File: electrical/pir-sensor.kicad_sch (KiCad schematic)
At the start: 6 parts, among them J6 0705430002

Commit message: Layout complete
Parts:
- J6: FT Rotation Offset (none) -> 90
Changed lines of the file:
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@@
 			)
 		)
-		(property "Datasheet" ""
+		(property "Datasheet" "https://www.molex.com/pdm_docs/sd/705430001_sd.pdf"
 			(at 100.33 78.74 0)
 			(effects
@@
 			)
 		)
-		(property "Description" ""
+		(property "Description" "Connector Header Through Hole 3 position 0.100\" (2.54mm)"
 			(at 100.33 78.74 0)
 			(effects
@@
 			(at 100.33 78.74 0)
 			(effects
+				(font
+					(size 1.27 1.27)
+				)
+				(hide yes)
+			)
+		)
+		(property "FT Rotation Offset" "90"
+			(at 100.33 78.74 0)
+			(effects

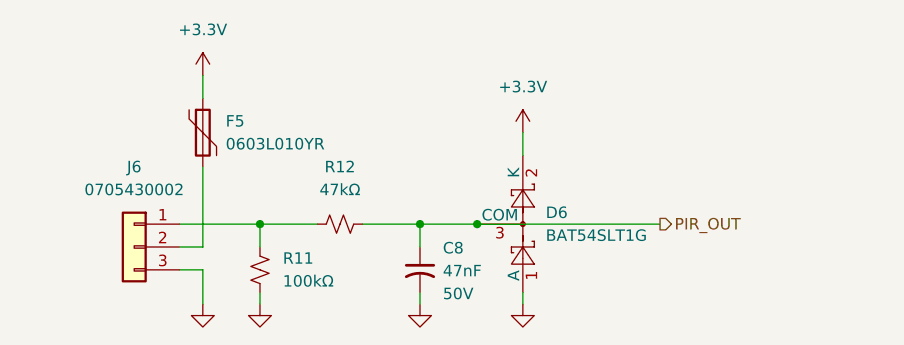
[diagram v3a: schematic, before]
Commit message: Finished and submitted to JLCPCB
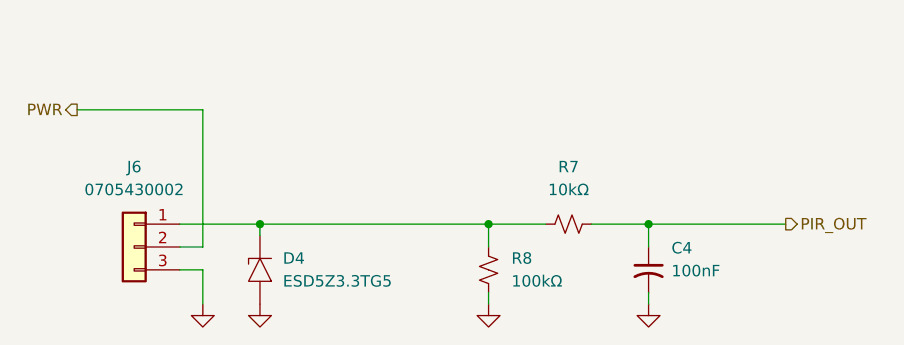
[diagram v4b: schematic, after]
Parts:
- removed D6: BAT54SLT1G, Package_TO_SOT_SMD:SOT-23, symbol !Diode:BAT54SLT1G
- removed F5: 0603L010YR, Fuse:Fuse_0603_1608Metric, symbol !Circuit Protection-Resettable Fuse:0603L010YR
- added D4: ESD5Z3.3TG5, Diode_SMD:D_SOD-523, symbol !Circuit Protection-ESD+TVS:ESD5Z3.3TG5
- C4: renamed from C8; value 47nF -> 100nF; symbol !Capacitor-0603:47nF_X7R_50V -> !Capacitor-0603:100nF_X7R_50V; JLCPCB PN C1622 -> C14663
- R7: renamed from R12; value 47kΩ -> 10kΩ; symbol !Resistor-0603:47kΩ -> !Resistor-0603:10kΩ; JLCPCB PN C25819 -> C25804
- renumbered R11 to R8
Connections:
- net GND: now also D4.2 (A)
- net at J6.1 (Pin_1), R7.1, R8.1: now also D4.1 (K1)
- net PWR: now reaches J6.2 (Pin_2)
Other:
- moved on the sheet: C4, R7, R8
